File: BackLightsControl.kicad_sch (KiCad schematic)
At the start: 0 parts

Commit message: Integration of changes into prewious style of schematic
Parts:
- added C53, C54, C55, C56, C57, C58: 100nF, PCM_JLCPCB:C_0805, symbol PCM_JLCPCB-Capacitors:0805,100nF,(2)
- added D14: BAT54S_C7420333, PCM_JLCPCB:SOT-23-3_L2.9-W1.3-P1.90-LS2.4-BR, symbol PCM_JLCPCB-Diode-Packages:Schottky, BAT54S_C7420333
- added D15: 1N4148W, PCM_JLCPCB:D_SOD-123, symbol PCM_JLCPCB-Diodes:Switching,1N4148W
- added J10: (no value), symbol JST_JWPF:B04B-JWPF-SK-R
- added J8: (no value), symbol JST_JWPF:B02B-JWPF-SK-R
- added J9: Conn_01x09, symbol Connector_Generic:Conn_01x09
- added R40, R41, R42, R43, R44, R45: 1kΩ, PCM_JLCPCB:R_0805, symbol PCM_JLCPCB-Resistors:0805,1kΩ
- added R46: 4.7kΩ, PCM_JLCPCB:R_0805, symbol PCM_JLCPCB-Resistors:0805,4.7kΩ
- added U10, U11, U12, U13, U14, U9: VND7050AJTR, easyeda2kicad:POWERSSO-16_L4.9-W3.9-P0.50-LS6.0-BL-EP, symbol easyeda2kicad:VND7050AJTR
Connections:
- new net: R41.2, U10.2 (~{FaultRST}), U11.2 (~{FaultRST}), U12.2 (~{FaultRST}), U13.2 (~{FaultRST}), U14.2 (~{FaultRST}), U9.2 (~{FaultRST})
- new net: D15.2, R46.1, U10.4 (GND), U11.4 (GND), U12.4 (GND), U13.4 (GND), U14.4 (GND), U9.4 (GND)
- new net: R42.2, U10.5 (SEL0), U11.5 (SEL0), U12.5 (SEL0), U13.5 (SEL0), U14.5 (SEL0), U9.5 (SEL0)
- new net: R43.2, U10.6 (SEL1), U11.6 (SEL1), U12.6 (SEL1), U13.6 (SEL1), U14.6 (SEL1), U9.6 (SEL1)
- new net: R44.2, R45.1, U10.7 (MultiSense), U11.7 (MultiSense), U12.7 (MultiSense), U13.7 (MultiSense), U14.7 (MultiSense), U9.7 (MultiSense)
- new net: J10.1, U13.10 (OUTPUT1), U13.11 (OUTPUT1), U13.12 (OUTPUT1), U13.9 (OUTPUT1)
- new net: J10.2, U14.13 (OUTPUT0), U14.14 (OUTPUT0), U14.15 (OUTPUT0), U14.16 (OUTPUT0)
- new net: J10.3, U14.10 (OUTPUT1), U14.11 (OUTPUT1), U14.12 (OUTPUT1), U14.9 (OUTPUT1)
- new net: J9.5 (Pin_5), U11.13 (OUTPUT0), U11.14 (OUTPUT0), U11.15 (OUTPUT0), U11.16 (OUTPUT0)
- new net: J9.6 (Pin_6), U11.10 (OUTPUT1), U11.11 (OUTPUT1), U11.12 (OUTPUT1), U11.9 (OUTPUT1)
- new net: J9.7 (Pin_7), U12.13 (OUTPUT0), U12.14 (OUTPUT0), U12.15 (OUTPUT0), U12.16 (OUTPUT0)
- new net: J9.8 (Pin_8), U12.10 (OUTPUT1), U12.11 (OUTPUT1), U12.12 (OUTPUT1), U12.9 (OUTPUT1)
- new net: J9.9 (Pin_9), U13.13 (OUTPUT0), U13.14 (OUTPUT0), U13.15 (OUTPUT0), U13.16 (OUTPUT0)
- new net +12V: C53.1, C54.1, C55.1, C56.1, C57.1, C58.1, U10.17 (VCC), U11.17 (VCC), U12.17 (VCC), U13.17 (VCC), U14.17 (VCC), U9.17 (VCC)
- new net +3.3V: D14.2 (K2), R40.2
- new net CargoCompLampOUT: J8.2, U9.13 (OUTPUT0), U9.14 (OUTPUT0), U9.15 (OUTPUT0), U9.16 (OUTPUT0)
- new net GND: C53.2, C54.2, C55.2, C56.2, C57.2, C58.2, D14.1 (K1), D15.1, J10.4, J8.1, J9.1 (Pin_1), R45.2, R46.2
- new net RearDirLampLeftOUT: J9.3 (Pin_3), U10.13 (OUTPUT0), U10.14 (OUTPUT0), U10.15 (OUTPUT0), U10.16 (OUTPUT0)
- new net RearDirLampRightOUT: J9.2 (Pin_2), U9.10 (OUTPUT1), U9.11 (OUTPUT1), U9.12 (OUTPUT1), U9.9 (OUTPUT1)
- new net SEL0: R42.1
- new net SEL1: R43.1
- new net Sense: D14.3 (A), R44.1
- new net StopLampOUT: J9.4 (Pin_4), U10.10 (OUTPUT1), U10.11 (OUTPUT1), U10.12 (OUTPUT1), U10.9 (OUTPUT1)
- new net output12: U9.1 (INPUT0)
- new net output13: U9.8 (INPUT1)
- new net output14: U10.1 (INPUT0)
- new net output15: U10.8 (INPUT1)
- new net output16: U11.1 (INPUT0)
- new net output17: U11.8 (INPUT1)
- new net output18: U12.1 (INPUT0)
- new net output19: U12.8 (INPUT1)
- new net output20: U13.1 (INPUT0)
- new net output21: U13.8 (INPUT1)
- new net output22: U14.1 (INPUT0)
- new net output23: U14.8 (INPUT1)
- new net selG: U9.3 (SEn)
- new net selH: U10.3 (SEn)
- new net selI: U11.3 (SEn)
- new net selJ: U12.3 (SEn)
- new net selK: U13.3 (SEn)
- new net selL: U14.3 (SEn)
- new net ~{FaultRST}: R40.1, R41.1
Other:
- note added: "12*12mA = 144mA peak Diode = 150mA nominal"
- note added: "::::???????????::::::"
- note added: "Ground Rear direction-indicator lamp, right Rear direction-indicator lamp, left Stop lamp Rear position lamp Rear fog lamp Reversing lamp NA NA"
- note added: "Per datasheet"
- note added: "Tell-tale Driving-beam"
- note added: "Tell-tale direction-indicator left"
- note added: "Tell-tale direction-indicator right"
- note added: "cargo compartment lamp"
- note added: "tail connector"

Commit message: I/O Schematic rebuild from DRAFT by Nathann
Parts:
- U10, U11, U12, U13, U14, U9: footprint easyeda2kicad:POWERSSO-16_L4.9-W3.9-P0.50-LS6.0-BL-EP -> Package_SO:PowerSSO-16-1EP_3.9x4.9mm_P0.5mm_EP2.5x3.61mm
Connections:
- net TT-DirIndLeftOUT: now reaches J10.1, U13.10 (OUTPUT1), U13.11 (OUTPUT1), U13.12 (OUTPUT1), U13.9 (OUTPUT1)
- net TT-DrivingBeamOUT: now reaches J10.2, U14.13 (OUTPUT0), U14.14 (OUTPUT0), U14.15 (OUTPUT0), U14.16 (OUTPUT0)
- net TT-DirIndRightOUT: now reaches J10.3, U14.10 (OUTPUT1), U14.11 (OUTPUT1), U14.12 (OUTPUT1), U14.9 (OUTPUT1)
- net RearPosLampOUT: now reaches J9.5 (Pin_5), U11.13 (OUTPUT0), U11.14 (OUTPUT0), U11.15 (OUTPUT0), U11.16 (OUTPUT0)
- net RearFogLampOUT: now reaches J9.6 (Pin_6), U11.10 (OUTPUT1), U11.11 (OUTPUT1), U11.12 (OUTPUT1), U11.9 (OUTPUT1)
- net ReversingLampOUT: now reaches J9.7 (Pin_7), U12.13 (OUTPUT0), U12.14 (OUTPUT0), U12.15 (OUTPUT0), U12.16 (OUTPUT0)
- net Rezerved1OUT: now reaches J9.8 (Pin_8), U12.10 (OUTPUT1), U12.11 (OUTPUT1), U12.12 (OUTPUT1), U12.9 (OUTPUT1)
- net Reserved2OUT: now reaches J9.9 (Pin_9), U13.13 (OUTPUT0), U13.14 (OUTPUT0), U13.15 (OUTPUT0), U13.16 (OUTPUT0)
- net SEL0 renamed RearSEL0
- net SEL1 renamed RearSEL1
- net Sense renamed RearSense
- net output12 renamed CargoCompLamp
- net output13 renamed RearDirLampR
- net output14 renamed RearDirLampL
- net output15 renamed StopLamp
- net output16 renamed RearPosLamp
- net output17 renamed RearFogLamp
- net output18 renamed ReversingLamp
- net output19 renamed Reserved1
- net output20 renamed Reserved2
- net output21 renamed DirIndicatorL
- net output22 renamed DrivingBeam
- net output23 renamed DirIndicatorR
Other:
- note added: "Tel tail connector"
- note added: "cargo compartment lamp connector"
- note removed: "cargo compartment lamp"
- moved on the sheet: C53, C54, C55, C56, C57, C58, D14, D15, J10, J8, J9, R40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

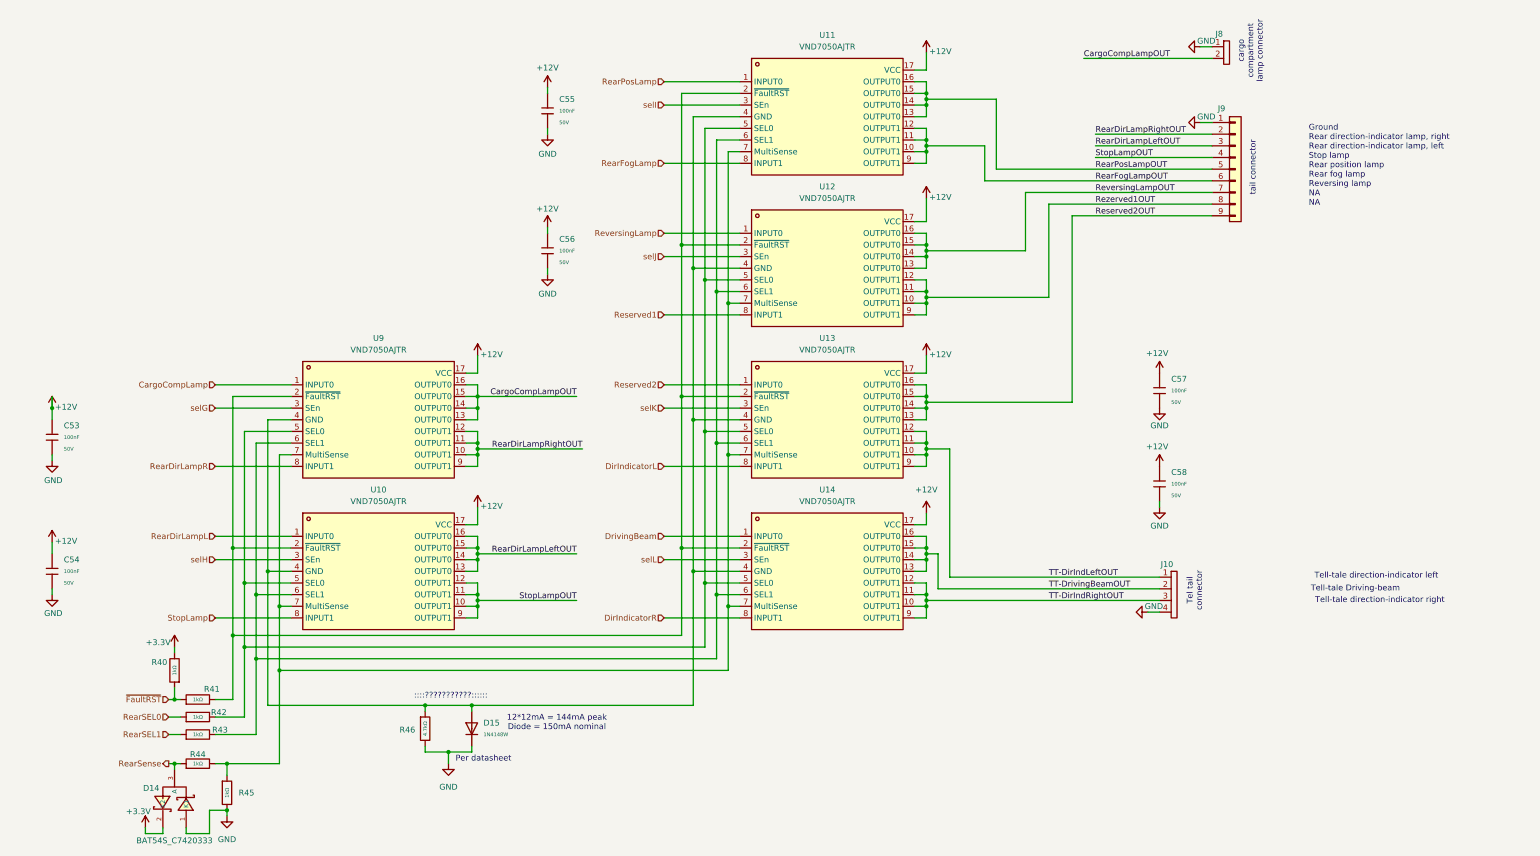
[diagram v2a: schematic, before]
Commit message: EMI/EMC meassures implementation + VCU panel interface block
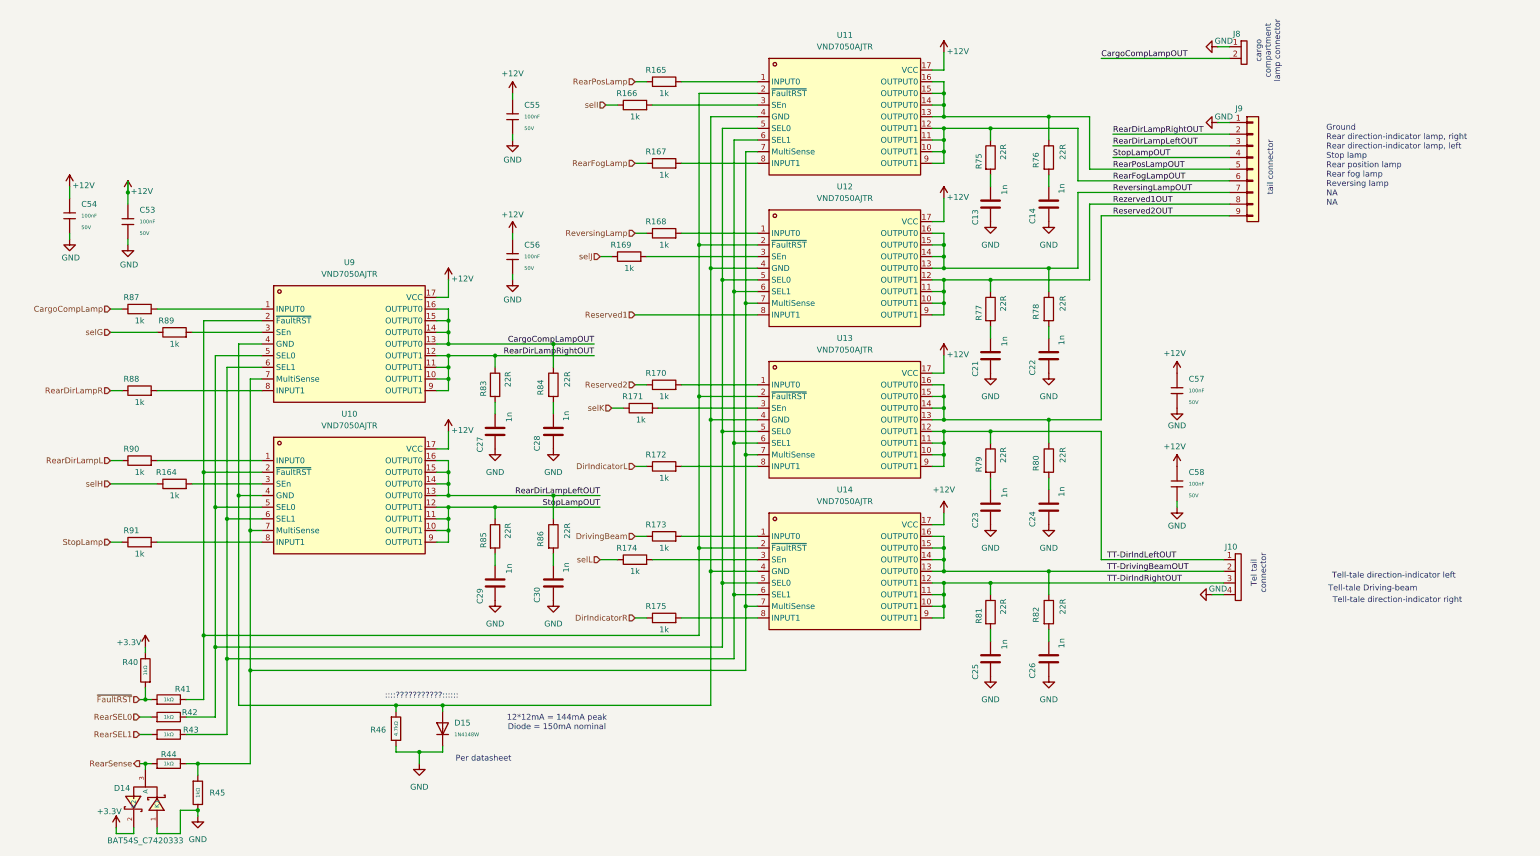
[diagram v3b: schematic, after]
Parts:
- added C13, C14, C21, C22, C23, C24, C25, C26, C27, C28, C29, C30: 1n, Capacitor_SMD:C_0603_1608Metric, symbol VELION_VCU_Library:C
- added R164, R165, R166, R167, R168, R169, R170, R171, R172, R173, R174, R175, R87, R88, R89, R90, R91: 1k, Resistor_SMD:R_0603_1608Metric, symbol VELION_VCU_Library:R
- added R75, R76, R77, R78, R79, R80, R81, R82, R83, R84, R85, R86: 22R, Resistor_SMD:R_0603_1608Metric, symbol VELION_VCU_Library:R
- C53, C54, C55, C56, C57, C58: footprint PCM_JLCPCB:C_0805 -> Capacitor_SMD:C_0603_1608Metric; symbol PCM_JLCPCB-Capacitors:0805,100nF,(2) -> VELION_VCU_Library:0805,100nF,(2)
- D14: footprint PCM_JLCPCB:SOT-23-3_L2.9-W1.3-P1.90-LS2.4-BR -> Package_TO_SOT_SMD:SOT-23-3; symbol PCM_JLCPCB-Diode-Packages:Schottky, BAT54S_C7420333 -> VELION_VCU_Library:Schottky, BAT54S_C7420333
- D15: footprint PCM_JLCPCB:D_SOD-123 -> Diode_SMD:D_SOD-123; symbol PCM_JLCPCB-Diodes:Switching,1N4148W -> VELION_VCU_Library:Switching,1N4148W
- J10: symbol JST_JWPF:B04B-JWPF-SK-R -> VELION_VCU_Library:B04B-JWPF-SK-R
- J8: symbol JST_JWPF:B02B-JWPF-SK-R -> VELION_VCU_Library:B02B-JWPF-SK-R
- J9: symbol Connector_Generic:Conn_01x09 -> VELION_VCU_Library:Conn_01x09
- R40, R41, R42, R43, R44, R45: footprint PCM_JLCPCB:R_0805 -> Resistor_SMD:R_0805_2012Metric; symbol PCM_JLCPCB-Resistors:0805,1kΩ -> VELION_VCU_Library:0805,1kΩ
- R46: footprint PCM_JLCPCB:R_0805 -> Resistor_SMD:R_0805_2012Metric; symbol PCM_JLCPCB-Resistors:0805,4.7kΩ -> VELION_VCU_Library:0805,4.7kΩ
- U10, U11, U12, U13, U14, U9: symbol easyeda2kicad:VND7050AJTR -> VELION_VCU_Library:VND7050AJTR
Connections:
- net CargoCompLamp: now also R87.1; no longer U9.1 (INPUT0)
- net CargoCompLampOUT: now also R84.1
- net DirIndicatorL: now also R172.1; no longer U13.8 (INPUT1)
- net DirIndicatorR: now also R175.1; no longer U14.8 (INPUT1)
- net DrivingBeam: now also R173.1; no longer U14.1 (INPUT0)
- net GND: now also C13.2, C14.2, C21.2, C22.2, C23.2, C24.2, C25.2, C26.2, C27.2, C28.2, C29.2, C30.2
- net RearDirLampL: now also R90.1; no longer U10.1 (INPUT0)
- net RearDirLampLeftOUT: now also R86.1
- net RearDirLampR: now also R88.1; no longer U9.8 (INPUT1)
- net RearDirLampRightOUT: now also R83.1
- net RearFogLamp: now also R167.1; no longer U11.8 (INPUT1)
- net RearFogLampOUT: now also R75.1
- net RearPosLamp: now also R165.1; no longer U11.1 (INPUT0)
- net RearPosLampOUT: now also R76.1
- net Reserved2: now also R170.1; no longer U13.1 (INPUT0)
- net Reserved2OUT: now also R80.1
- net ReversingLamp: now also R168.1; no longer U12.1 (INPUT0)
- net ReversingLampOUT: now also R78.1
- net Rezerved1OUT: now also R77.1
- net StopLamp: now also R91.1; no longer U10.8 (INPUT1)
- net StopLampOUT: now also R85.1
- net TT-DirIndLeftOUT: now also R79.1
- net TT-DirIndRightOUT: now also R81.1
- net TT-DrivingBeamOUT: now also R82.1
- net selG: now also R89.1; no longer U9.3 (SEn)
- net selH: now also R164.1; no longer U10.3 (SEn)
- net selI: now also R166.1; no longer U11.3 (SEn)
- net selJ: now also R169.1; no longer U12.3 (SEn)
- net selK: now also R171.1; no longer U13.3 (SEn)
- net selL: now also R174.1; no longer U14.3 (SEn)
- new net: C13.1, R75.2
- new net: R87.2, U9.1 (INPUT0)
- new net: R89.2, U9.3 (SEn)
- new net: R88.2, U9.8 (INPUT1)
- new net: R173.2, U14.1 (INPUT0)
- new net: C23.1, R79.2
- new net: R170.2, U13.1 (INPUT0)
- new net: C30.1, R86.2
- new net: R164.2, U10.3 (SEn)
- new net: R165.2, U11.1 (INPUT0)
- new net: C24.1, R80.2
- new net: C22.1, R78.2
- new net: R166.2, U11.3 (SEn)
- new net: C21.1, R77.2
- new net: R91.2, U10.8 (INPUT1)
- new net: R172.2, U13.8 (INPUT1)
- new net: C27.1, R83.2
- new net: C26.1, R82.2
- new net: R90.2, U10.1 (INPUT0)
- new net: R169.2, U12.3 (SEn)
- new net: R174.2, U14.3 (SEn)
- new net: C29.1, R85.2
- new net: R175.2, U14.8 (INPUT1)
- new net: C28.1, R84.2
- new net: R171.2, U13.3 (SEn)
- new net: R168.2, U12.1 (INPUT0)
- new net: C25.1, R81.2
- new net: R167.2, U11.8 (INPUT1)
- new net: C14.1, R76.2
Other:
- moved on the sheet: C53, C54, C55, C56, C57, C58, D14, D15, J10, J8, J9, R40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
